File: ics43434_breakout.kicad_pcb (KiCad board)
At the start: 2 copper layers, 10.7 x 8.1 mm, 5 parts, among them J1 Conn_01x03_Male, J2 Conn_01x03_Male, U1 ICS-43434

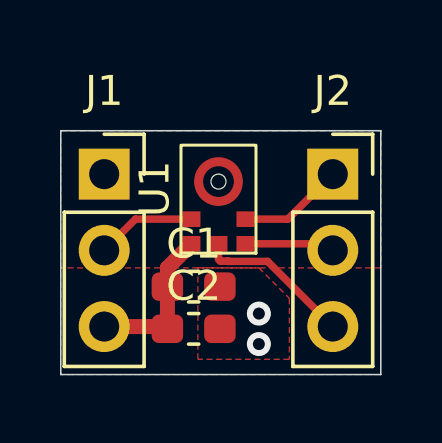
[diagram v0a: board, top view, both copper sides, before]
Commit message: update pcb
- add silkscreen pin functions
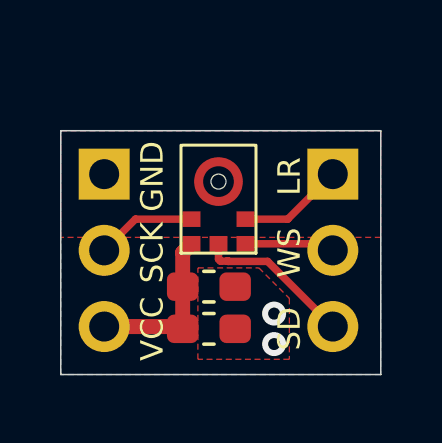
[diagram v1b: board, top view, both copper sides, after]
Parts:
- moved C1 0.51 mm to (103.5, 103.8)
- moved C2 0.51 mm to (103.5, 105.2)
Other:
- board text added: "GND"
- board text added: "LR"
- board text added: "SCK"
- board text added: "SD"
- board text added: "VCC"
- board text added: "WS"

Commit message: add SD pull-down resistor
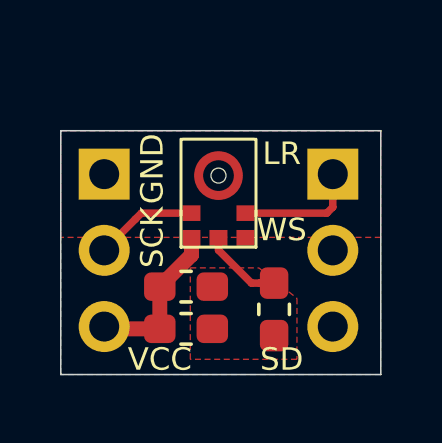
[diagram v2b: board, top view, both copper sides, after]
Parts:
- added R1: 100k, Resistor_SMD:R_0603_1608Metric_Pad1.05x0.95mm_HandSolder, F.Cu at (105.7, 104.5)
- moved C1 0.76 mm to (102.7, 103.8)
- moved C2 0.76 mm to (102.7, 105.2)
- moved U1 0.20 mm to (103.8, 101.3)
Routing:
- net /WS: track 3.00 -> 0.31 mm
- net /SD: track 5.30 -> 2.72 mm
- net /LR: track 3.53 -> 4.09 mm
- net GND: vias 2 -> 0
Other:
- board text added: "expoman ICS-43434 2020-01-23"
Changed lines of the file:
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@@
   (general
     (thickness 1.6)
-    (drawings 10)
-    (tracks 22)
+    (drawings 11)
+    (tracks 16)
     (zones 0)
-    (modules 5)
+    (modules 6)
     (nets 7)
   )
   (page A4)
   (layers
-    (0 F.Cu signal hide)
+    (0 F.Cu signal)
     (31 B.Cu signal hide)
     (32 B.Adhes user hide)
@@
     (37 F.SilkS user)
     (38 B.Mask user hide)
-    (39 F.Mask user)
+    (39 F.Mask user hide)
     (40 Dwgs.User user hide)
     (41 Cmts.User user hide)
@@
     (add_net VCC)
   )
+  (module Resistor_SMD:R_0603_1608Metric_Pad1.05x0.95mm_HandSolder (layer F.Cu)
+    (at 105.664 104.507 90)
+    (descr "Resistor SMD 0603 (1608 Metric), square (rectangular) end terminal, IPC_7351 nominal with elongated pad for handsoldering. (Body size source: http://www.tortai-tech.com/upload/download/2011102023233369053.pdf), generated with kicad-footprint-generator")
+    (tags "resistor handsolder")
+    (attr smd)
+    (fp_text reference R1 (at 0 -1.43 90) (layer F.SilkS) hide
+      (effects (font (size 1 1) (thickness 0.15)))
+    )
+    (fp_text value 100k (at 0 1.43 90) (layer F.Fab)
+      (effects (font (size 1 1) (thickness 0.15)))
+    )
+    (fp_text user %R (at 0 0 90) (layer F.Fab)
+      (effects (font (size 0.4 0.4) (thickness 0.06)))
+    )
+    (fp_line (start 1.65 0.73) (end -1.65 0.73) (layer F.CrtYd) (width 0.05))
+    (fp_line (start 1.65 -0.73) (end 1.65 0.73) (layer F.CrtYd) (width 0.05))
+    (fp_line (start -1.65 -0.73) (end 1.65 -0.73) (layer F.CrtYd) (width 0.05))
+    (fp_line (start -1.65 0.73) (end -1.65 -0.73) (layer F.CrtYd) (width 0.05))
+    (fp_line (start -0.171267 0.51) (end 0.171267 0.51) (layer F.SilkS) (width 0.12))
+    (fp_line (start -0.171267 -0.51) (end 0.171267 -0.51) (layer F.SilkS) (width 0.12))
+    (fp_line (start 0.8 0.4) (end -0.8 0.4) (layer F.Fab) (width 0.1))
+    (fp_line (start 0.8 -0.4) (end 0.8 0.4) (layer F.Fab) (width 0.1))
+    (fp_line (start -0.8 -0.4) (end 0.8 -0.4) (layer F.Fab) (width 0.1))
+    (fp_line (start -0.8 0.4) (end -0.8 -0.4) (layer F.Fab) (width 0.1))
+    (pad 2 smd roundrect (at 0.875 0 90) (size 1.05 0.95) (layers F.Cu F.Paste F.Mask) (roundrect_rratio 0.25)
+      (net 5 /SD))
+    (pad 1 smd roundrect (at -0.875 0 90) (size 1.05 0.95) (layers F.Cu F.Paste F.Mask) (roundrect_rratio 0.25)
+      (net 1 GND))
+    (model ${KISYS3DMOD}/Resistor_SMD.3dshapes/R_0603_1608Metric.wrl
+      (at (xyz 0 0 0))
+      (scale (xyz 1 1 1))
+      (rotate (xyz 0 0 0))
+    )
+  )
   (module Connector_PinSocket_2.54mm:PinSocket_1x03_P2.54mm_Vertical (layer F.Cu)
     (at 100 100)
@@
   )
   (module Sensor_Audio:TDK_ICS-43434 (layer F.Cu)
-    (at 103.81 101.5 90)
+    (at 103.81 101.3 90)
     (fp_text reference U1 (at 1.01 -2.13 90) (layer F.SilkS) hide
       (effects (font (size 1 1) (thickness 0.15)))
@@
   )
   (module Capacitor_SMD:C_0603_1608Metric_Pad1.05x0.95mm_HandSolder (layer F.Cu)
-    (at 103.491 105.156)
+    (at 102.729 105.156)
     (descr "Capacitor SMD 0603 (1608 Metric), square (rectangular) end terminal, IPC_7351 nominal with elongated pad for handsoldering. (Body size source: http://www.tortai-tech.com/upload/download/2011102023233369053.pdf), generated with kicad-footprint-generator")
     (tags "capacitor handsolder")
@@
   )
   (module Capacitor_SMD:C_0603_1608Metric_Pad1.05x0.95mm_HandSolder (layer F.Cu)
-    (at 103.491 103.75)
+    (at 102.729 103.75)
     (descr "Capacitor SMD 0603 (1608 Metric), square (rectangular) end terminal, IPC_7351 nominal with elongated pad for handsoldering. (Body size source: http://www.tortai-tech.com/upload/download/2011102023233369053.pdf), generated with kicad-footprint-generator")
     (tags "capacitor handsolder")
@@
     )
   )
-  (gr_text GND (at 101.6 100.076 90) (layer F.SilkS)
-    (effects (font (size 0.75 0.75) (thickness 0.15)))
-  )
-  (gr_text SCK (at 101.6 102.616 90) (layer F.SilkS)
-    (effects (font (size 0.75 0.75) (thickness 0.15)))
-  )
-  (gr_text VCC (at 101.6 105.156 90) (layer F.SilkS)
-    (effects (font (size 0.75 0.75) (thickness 0.15)))
-  )
-  (gr_text LR (at 106.172 100.076 90) (layer F.SilkS)
-    (effects (font (size 0.75 0.75) (thickness 0.15)))
-  )
-  (gr_text WS (at 106.172 102.616 90) (layer F.SilkS)
-    (effects (font (size 0.75 0.75) (thickness 0.15)))
-  )
-  (gr_text SD (at 106.172 105.156 90) (layer F.SilkS)
+  (gr_text "expoman\nICS-43434\n2020-01-23" (at 103.632 102.616) (layer B.SilkS)
+    (effects (font (size 0.5 0.5) (thickness 0.125)) (justify mirror))
+  )
+  (gr_text GND (at 101.6 99.822 90) (layer F.SilkS)
+    (effects (font (size 0.75 0.75) (thickness 0.15)))
+  )
+  (gr_text SCK (at 101.6 102.108 90) (layer F.SilkS)
+    (effects (font (size 0.75 0.75) (thickness 0.15)))
+  )
+  (gr_text VCC (at 101.854 106.172) (layer F.SilkS)
+    (effects (font (size 0.75 0.75) (thickness 0.15)))
+  )
+  (gr_text LR (at 105.918 99.314) (layer F.SilkS)
+    (effects (font (size 0.75 0.75) (thickness 0.15)))
+  )
+  (gr_text WS (at 105.918 101.854) (layer F.SilkS)
+    (effects (font (size 0.75 0.75) (thickness 0.15)))
+  )
+  (gr_text SD (at 105.918 106.172) (layer F.SilkS)
     (effects (font (size 0.75 0.75) (thickness 0.15)))
   )
@@
   (gr_line (start 98.552 106.68) (end 109.22 106.68) (layer Edge.Cuts) (width 0.05))
   (gr_line (start 98.552 98.552) (end 98.552 106.68) (layer Edge.Cuts) (width 0.05))
-  (via (at 105.664 105.664) (size 0.8) (drill 0.4) (layers F.Cu B.Cu) (net 1))
-  (via (at 105.664 104.648) (size 0.8) (drill 0.4) (layers F.Cu B.Cu) (net 1))
-  (segment (start 102.54 105.08) (end 102.616 105.156) (width 0.5) (layer F.Cu) (net 2))
-  (segment (start 100 105.08) (end 102.54 105.08) (width 0.5) (layer F.Cu) (net 2))
-  (segment (start 102.616 105.156) (end 102.616 103.75) (width 0.5) (layer F.Cu) (net 2))
-  (segment (start 102.616 102.616) (end 102.91 102.322) (width 0.5) (layer F.Cu) (net 2))
-  (segment (start 102.616 103.75) (end 102.616 102.616) (width 0.5) (layer F.Cu) (net 2))
+  (segment (start 102.91 102.694) (end 101.854 103.75) (width 0.5) (layer F.Cu) (net 2))
+  (segment (start 102.91 102.122) (end 102.91 102.694) (width 0.5) (layer F.Cu) (net 2))
+  (segment (start 101.854 103.75) (end 101.854 105.156) (width 0.5) (layer F.Cu) (net 2))
+  (segment (start 100.076 105.156) (end 100 105.08) (width 0.5) (layer F.Cu) (net 2))
+  (segment (start 101.854 105.156) (end 100.076 105.156) (width 0.5) (layer F.Cu) (net 2))
   (segment (start 107.402 102.322) (end 107.62 102.54) (width 0.25) (layer F.Cu) (net 3))
-  (segment (start 104.71 102.322) (end 107.402 102.322) (width 0.25) (layer F.Cu) (net 3))
-  (segment (start 101.04 101.5) (end 102.91 101.5) (width 0.25) (layer F.Cu) (net 4))
   (segment (start 100 102.54) (end 101.04 101.5) (width 0.25) (layer F.Cu) (net 4))
-  (segment (start 103.87699 102.89999) (end 104.1025 102.89999) (width 0.25) (layer F.Cu) (net 5))
-  (segment (start 103.81 102.322) (end 103.81 102.833) (width 0.25) (layer F.Cu) (net 5))
-  (segment (start 103.81 102.833) (end 103.87699 102.89999) (width 0.25) (layer F.Cu) (net 5))
-  (segment (start 104.141988 102.89999) (end 104.149999 102.908001) (width 0.25) (layer F.Cu) (net 5))
-  (segment (start 104.1025 102.89999) (end 104.141988 102.89999) (width 0.25) (layer F.Cu) (net 5))
-  (segment (start 104.110511 102.908001) (end 104.149999 102.908001) (width 0.25) (layer F.Cu) (net 5))
-  (segment (start 104.1025 102.89999) (end 104.110511 102.908001) (width 0.25) (layer F.Cu) (net 5))
-  (segment (start 105.448001 102.908001) (end 107.62 105.08) (width 0.25) (layer F.Cu) (net 5))
-  (segment (start 104.149999 102.908001) (end 105.448001 102.908001) (width 0.25) (layer F.Cu) (net 5))
-  (segment (start 106.12 101.5) (end 107.62 100) (width 0.25) (layer F.Cu) (net 6))
-  (segment (start 104.71 101.5) (end 106.12 101.5) (width 0.25) (layer F.Cu) (net 6))
+  (segment (start 101.24 101.3) (end 101.04 101.5) (width 0.25) (layer F.Cu) (net 4))
+  (segment (start 102.91 101.3) (end 101.24 101.3) (width 0.25) (layer F.Cu) (net 4))
+  (segment (start 105.189 103.632) (end 105.664 103.632) (width 0.25) (layer F.Cu) (net 5))
+  (segment (start 104.909 103.632) (end 105.189 103.632) (width 0.25) (layer F.Cu) (net 5))
+  (segment (start 103.81 102.533) (end 104.909 103.632) (width 0.25) (layer F.Cu) (net 5))
+  (segment (start 103.81 102.122) (end 103.81 102.533) (width 0.25) (layer F.Cu) (net 5))
+  (segment (start 107.42 101.3) (end 107.62 101.1) (width 0.25) (layer F.Cu) (net 6))
+  (segment (start 107.62 101.1) (end 107.62 100) (width 0.25) (layer F.Cu) (net 6))
+  (segment (start 104.71 101.3) (end 107.42 101.3) (width 0.25) (layer F.Cu) (net 6))
   (zone (net 1) (net_name GND) (layer B.Cu) (hatch edge 0.508)
     (connect_pads yes (clearance 0.254))
@@
     (polygon
       (pts
-        (xy 106.172 104.14) (xy 106.172 106.172) (xy 103.124 106.172) (xy 103.124 103.124) (xy 105.156 103.124)
+        (xy 106.426 104.14) (xy 106.426 106.172) (xy 102.87 106.172) (xy 102.87 103.124) (xy 105.156 103.124)
       )
     )

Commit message: remove 10uF capacitor
adapt layout
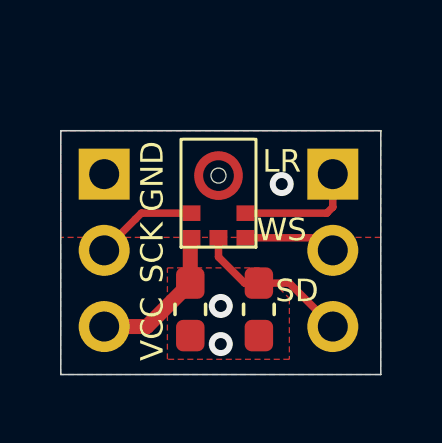
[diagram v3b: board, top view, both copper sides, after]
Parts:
- removed C2: 10uF, Capacitor_SMD:C_0603_1608Metric_Pad1.05x0.95mm_HandSolder
- moved C1 0.77 mm to (102.9, 104.5), turned to 270 degrees
- moved R1 0.51 mm to (105.2, 104.5)
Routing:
- net /WS: track 0.31 -> 3.39 mm
- net /SD: track 2.72 -> 5.41 mm
- net GND: vias 0 -> 3
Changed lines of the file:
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@@
     (thickness 1.6)
     (drawings 11)
-    (tracks 16)
+    (tracks 22)
     (zones 0)
-    (modules 6)
+    (modules 5)
     (nets 7)
   )
@@
   )
   (setup
-    (last_trace_width 0.5)
+    (last_trace_width 0.25)
     (user_trace_width 0.2)
     (user_trace_width 0.25)
@@
   )
   (module Resistor_SMD:R_0603_1608Metric_Pad1.05x0.95mm_HandSolder (layer F.Cu)
-    (at 105.664 104.507 90)
+    (at 105.156 104.507 90)
     (descr "Resistor SMD 0603 (1608 Metric), square (rectangular) end terminal, IPC_7351 nominal with elongated pad for handsoldering. (Body size source: http://www.tortai-tech.com/upload/download/2011102023233369053.pdf), generated with kicad-footprint-generator")
     (tags "resistor handsolder")
@@
   )
   (module Capacitor_SMD:C_0603_1608Metric_Pad1.05x0.95mm_HandSolder (layer F.Cu)
-    (at 102.729 105.156)
+    (at 102.87 104.507 270)
     (descr "Capacitor SMD 0603 (1608 Metric), square (rectangular) end terminal, IPC_7351 nominal with elongated pad for handsoldering. (Body size source: http://www.tortai-tech.com/upload/download/2011102023233369053.pdf), generated with kicad-footprint-generator")
     (tags "capacitor handsolder")
     (attr smd)
-    (fp_text reference C2 (at 1.665 0.508) (layer F.SilkS) hide
-      (effects (font (size 1 1) (thickness 0.15)))
-    )
-    (fp_text value 10uF (at 0 1.43) (layer F.Fab)
-      (effects (font (size 1 1) (thickness 0.15)))
-    )
-    (fp_text user %R (at 0 0) (layer F.Fab)
+    (fp_text reference C1 (at 0 -1.43 90) (layer F.SilkS) hide
+      (effects (font (size 1 1) (thickness 0.15)))
+    )
+    (fp_text value 100nF (at 0 1.43 90) (layer F.Fab)
+      (effects (font (size 1 1) (thickness 0.15)))
+    )
+    (fp_text user %R (at 0 0 90) (layer F.Fab)
       (effects (font (size 0.4 0.4) (thickness 0.06)))
     )
@@
     (fp_line (start -0.8 -0.4) (end 0.8 -0.4) (layer F.Fab) (width 0.1))
     (fp_line (start -0.8 0.4) (end -0.8 -0.4) (layer F.Fab) (width 0.1))
-    (pad 2 smd roundrect (at 0.875 0) (size 1.05 0.95) (layers F.Cu F.Paste F.Mask) (roundrect_rratio 0.25)
+    (pad 2 smd roundrect (at 0.875 0 270) (size 1.05 0.95) (layers F.Cu F.Paste F.Mask) (roundrect_rratio 0.25)
       (net 1 GND))
-    (pad 1 smd roundrect (at -0.875 0) (size 1.05 0.95) (layers F.Cu F.Paste F.Mask) (roundrect_rratio 0.25)
+    (pad 1 smd roundrect (at -0.875 0 270) (size 1.05 0.95) (layers F.Cu F.Paste F.Mask) (roundrect_rratio 0.25)
       (net 2 VCC))
     (model ${KISYS3DMOD}/Capacitor_SMD.3dshapes/C_0603_1608Metric.wrl
@@
     )
   )
-  (module Capacitor_SMD:C_0603_1608Metric_Pad1.05x0.95mm_HandSolder (layer F.Cu)
-    (at 102.729 103.75)
-    (descr "Capacitor SMD 0603 (1608 Metric), square (rectangular) end terminal, IPC_7351 nominal with elongated pad for handsoldering. (Body size source: http://www.tortai-tech.com/upload/download/2011102023233369053.pdf), generated with kicad-footprint-generator")
-    (tags "capacitor handsolder")
-    (attr smd)
-    (fp_text reference C1 (at 0 -1.43) (layer F.SilkS) hide
-      (effects (font (size 1 1) (thickness 0.15)))
-    )
-    (fp_text value 100nF (at 0 1.43) (layer F.Fab)
-      (effects (font (size 1 1) (thickness 0.15)))
-    )
-    (fp_text user %R (at 0 0) (layer F.Fab)
-      (effects (font (size 0.4 0.4) (thickness 0.06)))
-    )
-    (fp_line (start 1.65 0.73) (end -1.65 0.73) (layer F.CrtYd) (width 0.05))
-    (fp_line (start 1.65 -0.73) (end 1.65 0.73) (layer F.CrtYd) (width 0.05))
-    (fp_line (start -1.65 -0.73) (end 1.65 -0.73) (layer F.CrtYd) (width 0.05))
-    (fp_line (start -1.65 0.73) (end -1.65 -0.73) (layer F.CrtYd) (width 0.05))
-    (fp_line (start -0.171267 0.51) (end 0.171267 0.51) (layer F.SilkS) (width 0.12))
-    (fp_line (start -0.171267 -0.51) (end 0.171267 -0.51) (layer F.SilkS) (width 0.12))
-    (fp_line (start 0.8 0.4) (end -0.8 0.4) (layer F.Fab) (width 0.1))
-    (fp_line (start 0.8 -0.4) (end 0.8 0.4) (layer F.Fab) (width 0.1))
-    (fp_line (start -0.8 -0.4) (end 0.8 -0.4) (layer F.Fab) (width 0.1))
-    (fp_line (start -0.8 0.4) (end -0.8 -0.4) (layer F.Fab) (width 0.1))
-    (pad 2 smd roundrect (at 0.875 0) (size 1.05 0.95) (layers F.Cu F.Paste F.Mask) (roundrect_rratio 0.25)
-      (net 1 GND))
-    (pad 1 smd roundrect (at -0.875 0) (size 1.05 0.95) (layers F.Cu F.Paste F.Mask) (roundrect_rratio 0.25)
-      (net 2 VCC))
-    (model ${KISYS3DMOD}/Capacitor_SMD.3dshapes/C_0603_1608Metric.wrl
-      (at (xyz 0 0 0))
-      (scale (xyz 1 1 1))
-      (rotate (xyz 0 0 0))
-    )
-  )
   (gr_text "expoman\nICS-43434\n2020-01-23" (at 103.632 102.616) (layer B.SilkS)
     (effects (font (size 0.5 0.5) (thickness 0.125)) (justify mirror))
   )
-  (gr_text GND (at 101.6 99.822 90) (layer F.SilkS)
-    (effects (font (size 0.75 0.75) (thickness 0.15)))
-  )
-  (gr_text SCK (at 101.6 102.108 90) (layer F.SilkS)
-    (effects (font (size 0.75 0.75) (thickness 0.15)))
-  )
-  (gr_text VCC (at 101.854 106.172) (layer F.SilkS)
-    (effects (font (size 0.75 0.75) (thickness 0.15)))
-  )
-  (gr_text LR (at 105.918 99.314) (layer F.SilkS)
+  (gr_text GND (at 101.6 100.076 90) (layer F.SilkS)
+    (effects (font (size 0.75 0.75) (thickness 0.15)))
+  )
+  (gr_text SCK (at 101.6 102.616 90) (layer F.SilkS)
+    (effects (font (size 0.75 0.75) (thickness 0.15)))
+  )
+  (gr_text VCC (at 101.6 105.156 90) (layer F.SilkS)
+    (effects (font (size 0.75 0.75) (thickness 0.15)))
+  )
+  (gr_text LR (at 105.918 99.568) (layer F.SilkS)
     (effects (font (size 0.75 0.75) (thickness 0.15)))
   )
@@
     (effects (font (size 0.75 0.75) (thickness 0.15)))
   )
-  (gr_text SD (at 105.918 106.172) (layer F.SilkS)
+  (gr_text SD (at 106.426 103.886) (layer F.SilkS)
     (effects (font (size 0.75 0.75) (thickness 0.15)))
   )
@@
   (gr_line (start 98.552 106.68) (end 109.22 106.68) (layer Edge.Cuts) (width 0.05))
   (gr_line (start 98.552 98.552) (end 98.552 106.68) (layer Edge.Cuts) (width 0.05))
-  (segment (start 102.91 102.694) (end 101.854 103.75) (width 0.5) (layer F.Cu) (net 2))
-  (segment (start 102.91 102.122) (end 102.91 102.694) (width 0.5) (layer F.Cu) (net 2))
-  (segment (start 101.854 103.75) (end 101.854 105.156) (width 0.5) (layer F.Cu) (net 2))
+  (via (at 103.886 105.664) (size 0.8) (drill 0.4) (layers F.Cu B.Cu) (net 1))
+  (via (at 103.886 104.394) (size 0.8) (drill 0.4) (layers F.Cu B.Cu) (net 1))
+  (via (at 105.918 100.33) (size 0.8) (drill 0.4) (layers F.Cu B.Cu) (net 1))
   (segment (start 100.076 105.156) (end 100 105.08) (width 0.5) (layer F.Cu) (net 2))
-  (segment (start 101.854 105.156) (end 100.076 105.156) (width 0.5) (layer F.Cu) (net 2))
+  (segment (start 101.422 105.08) (end 102.87 103.632) (width 0.5) (layer F.Cu) (net 2))
+  (segment (start 100 105.08) (end 101.422 105.08) (width 0.5) (layer F.Cu) (net 2))
+  (segment (start 102.87 102.162) (end 102.91 102.122) (width 0.5) (layer F.Cu) (net 2))
+  (segment (start 102.87 103.632) (end 102.87 102.162) (width 0.5) (layer F.Cu) (net 2))
   (segment (start 107.402 102.322) (end 107.62 102.54) (width 0.25) (layer F.Cu) (net 3))
+  (segment (start 107.202 102.122) (end 107.62 102.54) (width 0.25) (layer F.Cu) (net 3))
+  (segment (start 104.71 102.122) (end 107.202 102.122) (width 0.25) (layer F.Cu) (net 3))
   (segment (start 100 102.54) (end 101.04 101.5) (width 0.25) (layer F.Cu) (net 4))
   (segment (start 101.24 101.3) (end 101.04 101.5) (width 0.25) (layer F.Cu) (net 4))
   (segment (start 102.91 101.3) (end 101.24 101.3) (width 0.25) (layer F.Cu) (net 4))
-  (segment (start 105.189 103.632) (end 105.664 103.632) (width 0.25) (layer F.Cu) (net 5))
-  (segment (start 104.909 103.632) (end 105.189 103.632) (width 0.25) (layer F.Cu) (net 5))
-  (segment (start 103.81 102.533) (end 104.909 103.632) (width 0.25) (layer F.Cu) (net 5))
-  (segment (start 103.81 102.122) (end 103.81 102.533) (width 0.25) (layer F.Cu) (net 5))
+  (segment (start 104.681 103.632) (end 105.156 103.632) (width 0.25) (layer F.Cu) (net 5))
+  (segment (start 103.81 102.761) (end 104.681 103.632) (width 0.25) (layer F.Cu) (net 5))
+  (segment (start 103.81 102.122) (end 103.81 102.761) (width 0.25) (layer F.Cu) (net 5))
+  (segment (start 106.172 103.632) (end 107.62 105.08) (width 0.25) (layer F.Cu) (net 5))
+  (segment (start 105.156 103.632) (end 106.172 103.632) (width 0.25) (layer F.Cu) (net 5))
   (segment (start 107.42 101.3) (end 107.62 101.1) (width 0.25) (layer F.Cu) (net 6))
   (segment (start 107.62 101.1) (end 107.62 100) (width 0.25) (layer F.Cu) (net 6))
@@
     (polygon
       (pts
-        (xy 106.426 104.14) (xy 106.426 106.172) (xy 102.87 106.172) (xy 102.87 103.124) (xy 105.156 103.124)
+        (xy 106.172 104.14) (xy 106.172 106.172) (xy 102.108 106.172) (xy 102.108 103.124) (xy 105.156 103.124)
       )
     )

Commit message: squeeze layout to 9.91x7.87mm
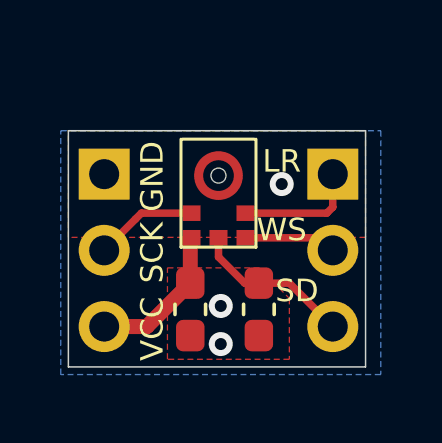
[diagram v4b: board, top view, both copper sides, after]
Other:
- board size 10.7 x 8.1 mm -> 9.9 x 7.9 mm
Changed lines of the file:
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@@
     (effects (font (size 0.75 0.75) (thickness 0.15)))
   )
-  (gr_line (start 109.22 98.552) (end 98.552 98.552) (layer Edge.Cuts) (width 0.05))
-  (gr_line (start 109.22 106.68) (end 109.22 98.552) (layer Edge.Cuts) (width 0.05))
-  (gr_line (start 98.552 106.68) (end 109.22 106.68) (layer Edge.Cuts) (width 0.05))
-  (gr_line (start 98.552 98.552) (end 98.552 106.68) (layer Edge.Cuts) (width 0.05))
+  (gr_line (start 108.712 98.552) (end 98.806 98.552) (layer Edge.Cuts) (width 0.05))
+  (gr_line (start 108.712 106.426) (end 108.712 98.552) (layer Edge.Cuts) (width 0.05))
+  (gr_line (start 98.806 106.426) (end 108.712 106.426) (layer Edge.Cuts) (width 0.05))
+  (gr_line (start 98.806 98.552) (end 98.806 106.426) (layer Edge.Cuts) (width 0.05))
   (via (at 103.886 105.664) (size 0.8) (drill 0.4) (layers F.Cu B.Cu) (net 1))
   (via (at 103.886 104.394) (size 0.8) (drill 0.4) (layers F.Cu B.Cu) (net 1))
@@
     (polygon
       (pts
-        (xy 109.22 102.108) (xy 98.552 102.108) (xy 98.552 98.552) (xy 109.22 98.552)
+        (xy 108.712 102.108) (xy 98.806 102.108) (xy 98.806 98.552) (xy 108.712 98.552)
       )
     )
